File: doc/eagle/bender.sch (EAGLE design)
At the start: 13 parts

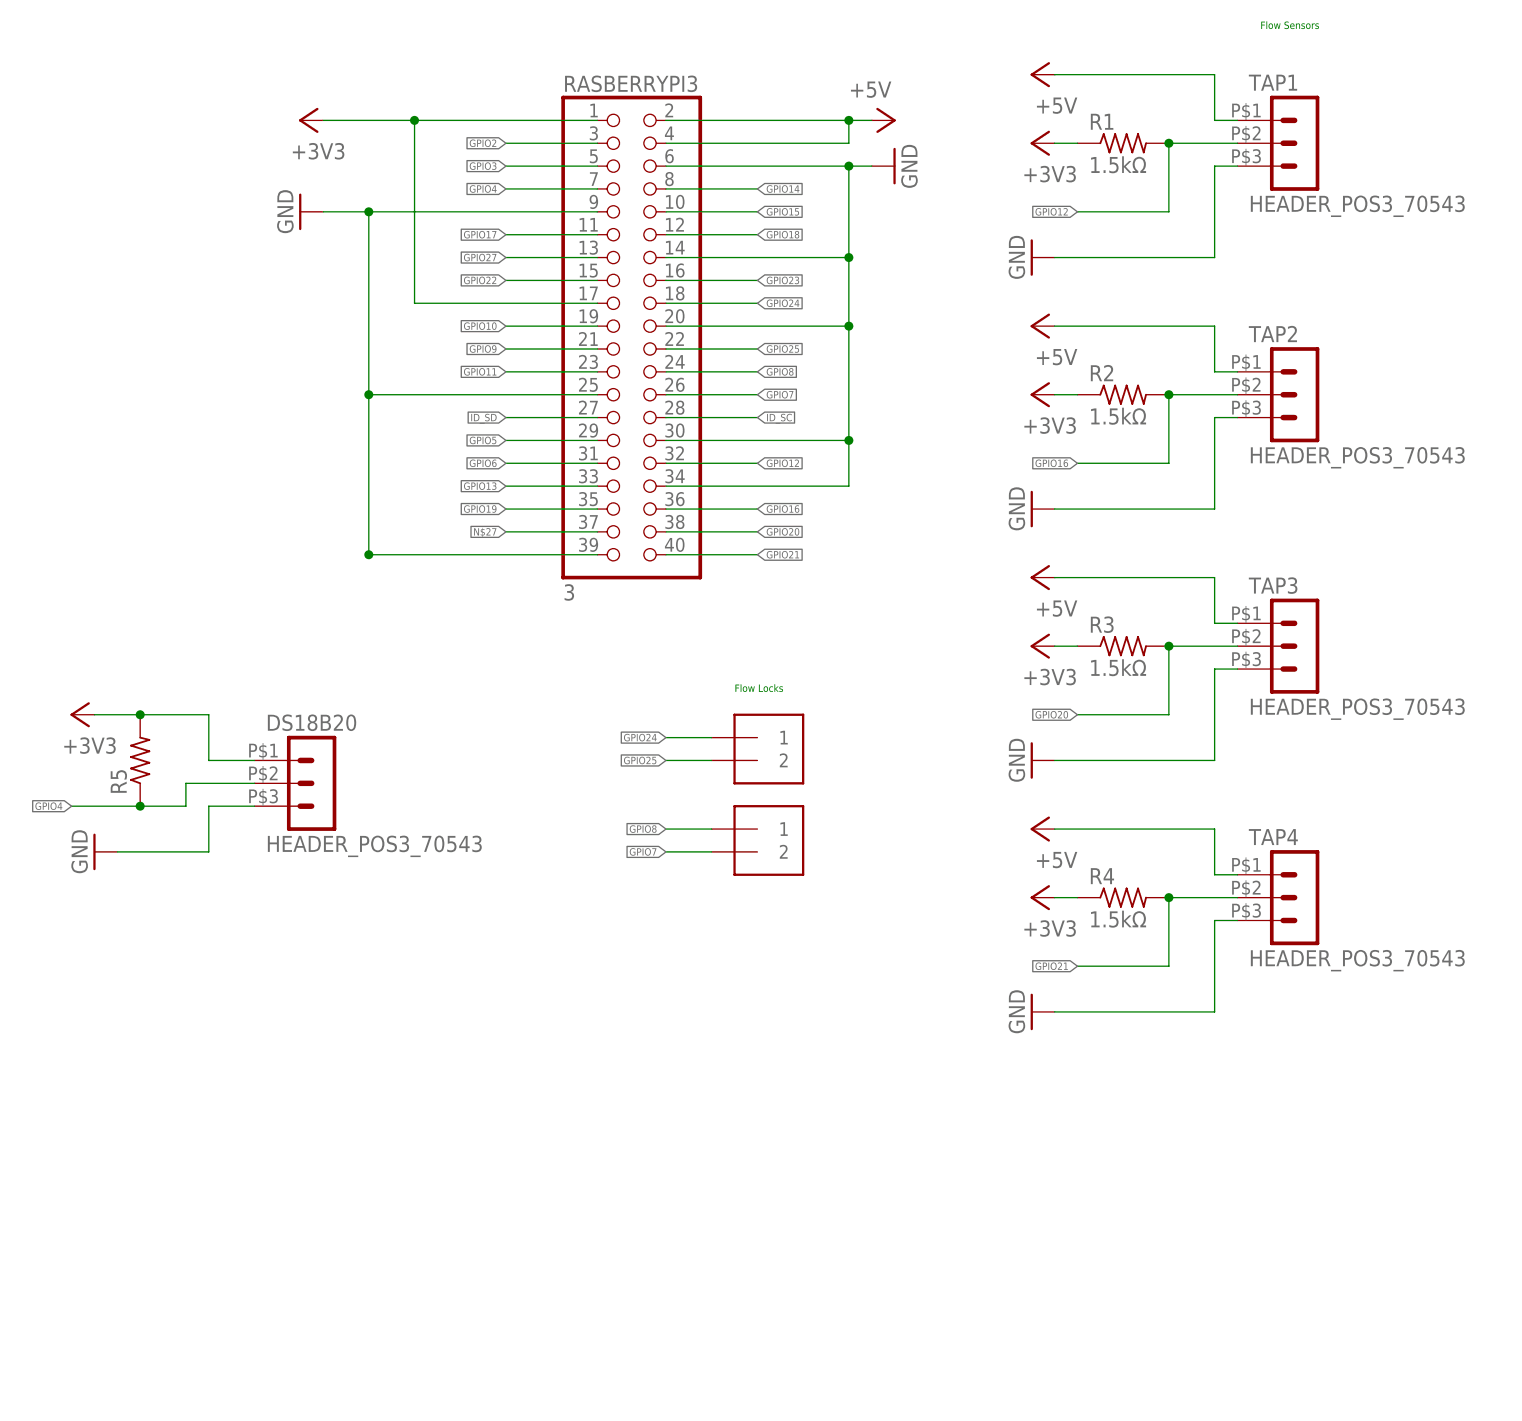
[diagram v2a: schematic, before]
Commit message: Updated schematic to reflect board.
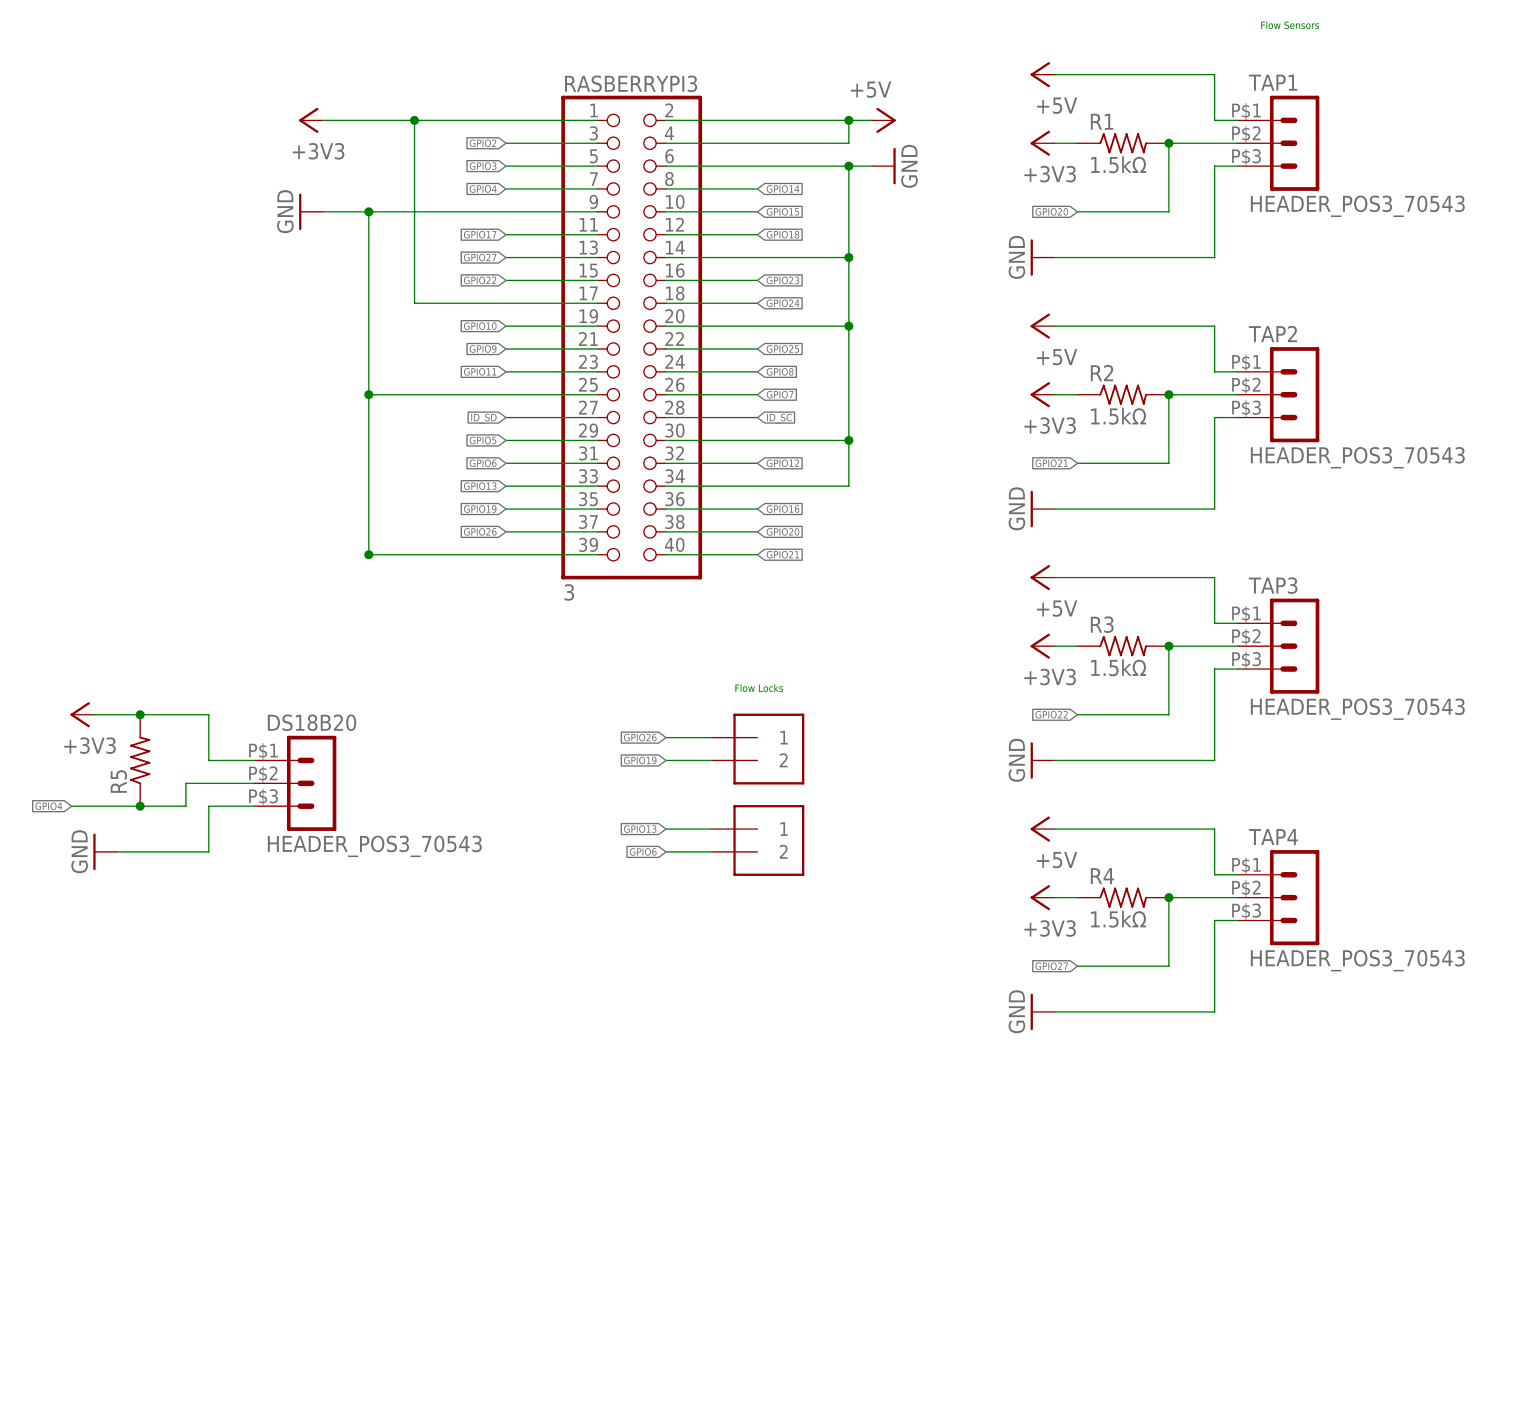
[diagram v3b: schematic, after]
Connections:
- removed net N$27: RASBERRYPI3.37
- new net GPIO26: LOCK12.1, RASBERRYPI3.37
- net GPIO12: no longer R1.2, TAP1.2
- net GPIO13: now also LOCK34.1
- net GPIO16: no longer R2.2, TAP2.2
- net GPIO19: now also LOCK12.2
- net GPIO20: now also R1.2, TAP1.2; no longer R3.2, TAP3.2
- net GPIO21: now also R2.2, TAP2.2; no longer R4.2, TAP4.2
- net GPIO22: now also R3.2, TAP3.2
- net GPIO24: no longer LOCK12.1
- net GPIO25: no longer LOCK12.2
- net GPIO27: now also R4.2, TAP4.2
- net GPIO6: now also LOCK34.2
- net GPIO7: no longer LOCK34.2
- net GPIO8: no longer LOCK34.1
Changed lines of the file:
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@@
 <label x="55.88" y="58.42" size="0.8128" layer="95" xref="yes"/>
-</segment>
-<segment>
-<pinref part="LOCK12" gate="G$1" pin="1"/>
-<wire x1="50.8" y1="10.16" x2="45.72" y2="10.16" width="0.1524" layer="91"/>
-<label x="45.72" y="10.16" size="0.8128" layer="95" rot="R180" xref="yes"/>
 </segment>
 </net>
@@
 <label x="55.88" y="53.34" size="0.8128" layer="95" xref="yes"/>
 </segment>
-<segment>
-<pinref part="LOCK12" gate="G$1" pin="2"/>
-<wire x1="50.8" y1="7.62" x2="45.72" y2="7.62" width="0.1524" layer="91"/>
-<label x="45.72" y="7.62" size="0.8128" layer="95" rot="R180" xref="yes"/>
-</segment>
 </net>
 <net name="GPIO8" class="0">
@@
 <label x="55.88" y="50.8" size="0.8128" layer="95" xref="yes"/>
 </segment>
-<segment>
-<pinref part="LOCK34" gate="G$1" pin="1"/>
-<wire x1="50.8" y1="0" x2="45.72" y2="0" width="0.1524" layer="91"/>
-<label x="45.72" y="0" size="0.8128" layer="95" rot="R180" xref="yes"/>
-</segment>
 </net>
 <net name="GPIO7" class="0">
@@
 <label x="55.88" y="48.26" size="0.8128" layer="95" xref="yes"/>
 </segment>
-<segment>
-<pinref part="LOCK34" gate="G$1" pin="2"/>
-<wire x1="50.8" y1="-2.54" x2="45.72" y2="-2.54" width="0.1524" layer="91"/>
-<label x="45.72" y="-2.54" size="0.8128" layer="95" rot="R180" xref="yes"/>
-</segment>
 </net>
 <net name="ID_SC" class="0">
@@
 <wire x1="45.72" y1="40.64" x2="55.88" y2="40.64" width="0.1524" layer="91"/>
 <label x="55.88" y="40.64" size="0.8128" layer="95" xref="yes"/>
+</segment>
+</net>
+<net name="GPIO16" class="0">
+<segment>
+<pinref part="RASBERRYPI3" gate="A" pin="36"/>
+<wire x1="45.72" y1="35.56" x2="55.88" y2="35.56" width="0.1524" layer="91"/>
+<label x="55.88" y="35.56" size="0.8128" layer="95" xref="yes"/>
+</segment>
+</net>
+<net name="GPIO20" class="0">
+<segment>
+<pinref part="RASBERRYPI3" gate="A" pin="38"/>
+<wire x1="45.72" y1="33.02" x2="55.88" y2="33.02" width="0.1524" layer="91"/>
+<label x="55.88" y="33.02" size="0.8128" layer="95" xref="yes"/>
 </segment>
 <segment>
@@
 </segment>
 </net>
-<net name="GPIO16" class="0">
-<segment>
-<pinref part="RASBERRYPI3" gate="A" pin="36"/>
-<wire x1="45.72" y1="35.56" x2="55.88" y2="35.56" width="0.1524" layer="91"/>
-<label x="55.88" y="35.56" size="0.8128" layer="95" xref="yes"/>
+<net name="GPIO21" class="0">
+<segment>
+<pinref part="RASBERRYPI3" gate="A" pin="40"/>
+<wire x1="45.72" y1="30.48" x2="55.88" y2="30.48" width="0.1524" layer="91"/>
+<label x="55.88" y="30.48" size="0.8128" layer="95" xref="yes"/>
 </segment>
 <segment>
@@
 <wire x1="101.6" y1="40.64" x2="91.44" y2="40.64" width="0.1524" layer="91"/>
 <label x="91.44" y="40.64" size="0.8128" layer="95" rot="R180" xref="yes"/>
-</segment>
-</net>
-<net name="GPIO20" class="0">
-<segment>
-<pinref part="RASBERRYPI3" gate="A" pin="38"/>
-<wire x1="45.72" y1="33.02" x2="55.88" y2="33.02" width="0.1524" layer="91"/>
-<label x="55.88" y="33.02" size="0.8128" layer="95" xref="yes"/>
-</segment>
-<segment>
-<pinref part="R3" gate="G$1" pin="2"/>
-<junction x="101.6" y="20.32"/>
-<pinref part="TAP3" gate="G$1" pin="2"/>
-<wire x1="109.22" y1="20.32" x2="101.6" y2="20.32" width="0.1524" layer="91"/>
-<wire x1="101.6" y1="20.32" x2="101.6" y2="12.7" width="0.1524" layer="91"/>
-<wire x1="101.6" y1="12.7" x2="91.44" y2="12.7" width="0.1524" layer="91"/>
-<label x="91.44" y="12.7" size="0.8128" layer="95" rot="R180" xref="yes"/>
-</segment>
-</net>
-<net name="GPIO21" class="0">
-<segment>
-<pinref part="RASBERRYPI3" gate="A" pin="40"/>
-<wire x1="45.72" y1="30.48" x2="55.88" y2="30.48" width="0.1524" layer="91"/>
-<label x="55.88" y="30.48" size="0.8128" layer="95" xref="yes"/>
-</segment>
-<segment>
-<pinref part="R4" gate="G$1" pin="2"/>
-<junction x="101.6" y="-7.62"/>
-<pinref part="TAP4" gate="G$1" pin="2"/>
-<wire x1="109.22" y1="-7.62" x2="101.6" y2="-7.62" width="0.1524" layer="91"/>
-<wire x1="101.6" y1="-7.62" x2="101.6" y2="-15.24" width="0.1524" layer="91"/>
-<wire x1="101.6" y1="-15.24" x2="91.44" y2="-15.24" width="0.1524" layer="91"/>
-<label x="91.44" y="-15.24" size="0.8128" layer="95" rot="R180" xref="yes"/>
 </segment>
 </net>
@@
 <label x="27.94" y="63.5" size="0.8128" layer="95" rot="R180" xref="yes"/>
 </segment>
+<segment>
+<pinref part="R4" gate="G$1" pin="2"/>
+<junction x="101.6" y="-7.62"/>
+<pinref part="TAP4" gate="G$1" pin="2"/>
+<wire x1="109.22" y1="-7.62" x2="101.6" y2="-7.62" width="0.1524" layer="91"/>
+<wire x1="101.6" y1="-7.62" x2="101.6" y2="-15.24" width="0.1524" layer="91"/>
+<wire x1="101.6" y1="-15.24" x2="91.44" y2="-15.24" width="0.1524" layer="91"/>
+<label x="91.44" y="-15.24" size="0.8128" layer="95" rot="R180" xref="yes"/>
+</segment>
 </net>
 <net name="GPIO22" class="0">
@@
 <label x="27.94" y="60.96" size="0.8128" layer="95" rot="R180" xref="yes"/>
 </segment>
+<segment>
+<pinref part="R3" gate="G$1" pin="2"/>
+<junction x="101.6" y="20.32"/>
+<pinref part="TAP3" gate="G$1" pin="2"/>
+<wire x1="109.22" y1="20.32" x2="101.6" y2="20.32" width="0.1524" layer="91"/>
+<wire x1="101.6" y1="20.32" x2="101.6" y2="12.7" width="0.1524" layer="91"/>
+<wire x1="101.6" y1="12.7" x2="91.44" y2="12.7" width="0.1524" layer="91"/>
+<label x="91.44" y="12.7" size="0.8128" layer="95" rot="R180" xref="yes"/>
+</segment>
 </net>
 <net name="GPIO10" class="0">
@@
 <label x="27.94" y="40.64" size="0.8128" layer="95" rot="R180" xref="yes"/>
 </segment>
+<segment>
+<pinref part="LOCK34" gate="G$1" pin="2"/>
+<wire x1="50.8" y1="-2.54" x2="45.72" y2="-2.54" width="0.1524" layer="91"/>
+<label x="45.72" y="-2.54" size="0.8128" layer="95" rot="R180" xref="yes"/>
+</segment>
 </net>
 <net name="GPIO13" class="0">
@@
 <label x="27.94" y="38.1" size="0.8128" layer="95" rot="R180" xref="yes"/>
 </segment>
+<segment>
+<pinref part="LOCK34" gate="G$1" pin="1"/>
+<wire x1="50.8" y1="0" x2="45.72" y2="0" width="0.1524" layer="91"/>
+<label x="45.72" y="0" size="0.8128" layer="95" rot="R180" xref="yes"/>
+</segment>
 </net>
 <net name="GPIO19" class="0">
@@
 <label x="27.94" y="35.56" size="0.8128" layer="95" rot="R180" xref="yes"/>
 </segment>
-</net>
-<net name="N$27" class="0">
+<segment>
+<pinref part="LOCK12" gate="G$1" pin="2"/>
+<wire x1="50.8" y1="7.62" x2="45.72" y2="7.62" width="0.1524" layer="91"/>
+<label x="45.72" y="7.62" size="0.8128" layer="95" rot="R180" xref="yes"/>
+</segment>
+</net>
+<net name="GPIO26" class="0">
 <segment>
 <pinref part="RASBERRYPI3" gate="A" pin="37"/>
@@
 <label x="27.94" y="33.02" size="0.8128" layer="95" rot="R180" xref="yes"/>
 </segment>
-</net>
+<segment>
+<pinref part="LOCK12" gate="G$1" pin="1"/>
+<wire x1="50.8" y1="10.16" x2="45.72" y2="10.16" width="0.1524" layer="91"/>
+<label x="45.72" y="10.16" size="0.8128" layer="95" rot="R180" xref="yes"/>
+</segment>
+</net>
